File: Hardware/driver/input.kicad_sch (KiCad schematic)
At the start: 55 parts, among them J301 1017526, Q301 IXTH80N075L2, Q302 IXTH80N075L2, U301 MCP3421A2T-ECH, U302 MCP3421A1T-ECH, U303 DAC60501Z, U304 DAC60501Z, U305 DS18B20, U306 DS18B20, U307 MCP3421A3T-ECH, U308 OPA2388, U309 OPA2388

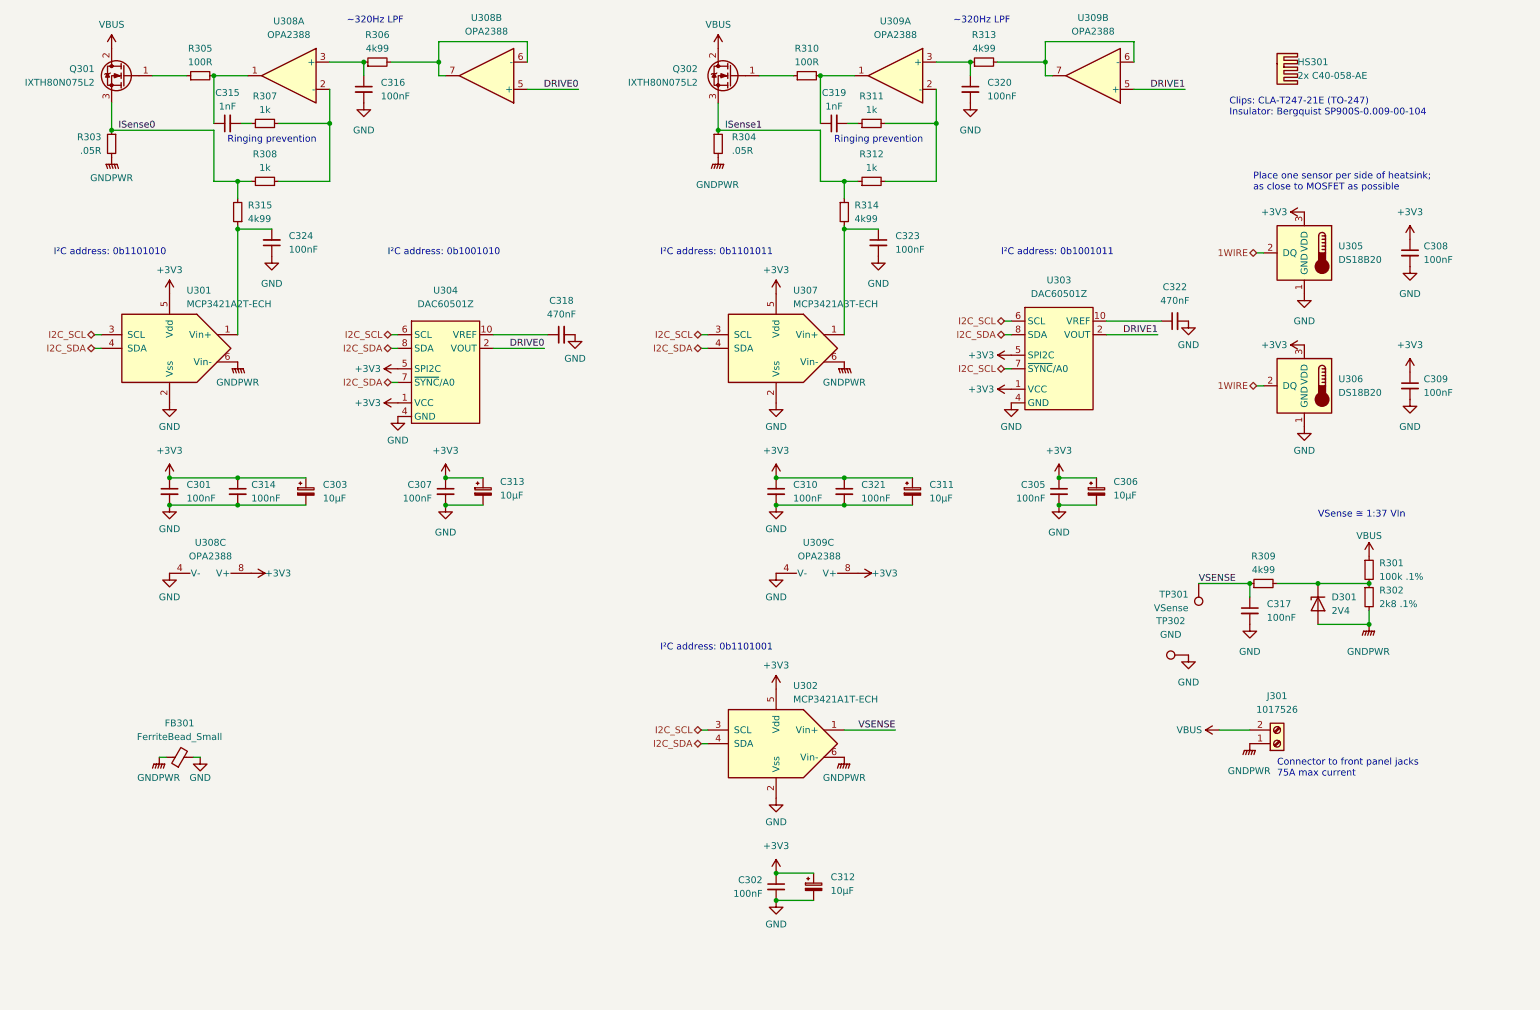
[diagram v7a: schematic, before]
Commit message: Driver current zero adjustment
- Added facility on the driver board to adjust the zero offset for the
  current drive op amps, to allow them to actually reach zero when a
  zero DAC code is input to them.

  This is done by means of a -5V supply (generated with switched
  capacitor regulator) and each output amplifier having a -2.5V
  reference, and an associated multi-turn trim pot to actually trim
  that; these are hooked up to 3V3 digital on the other end (this should
  probably be the DAC reference but we don't have ez access to that)
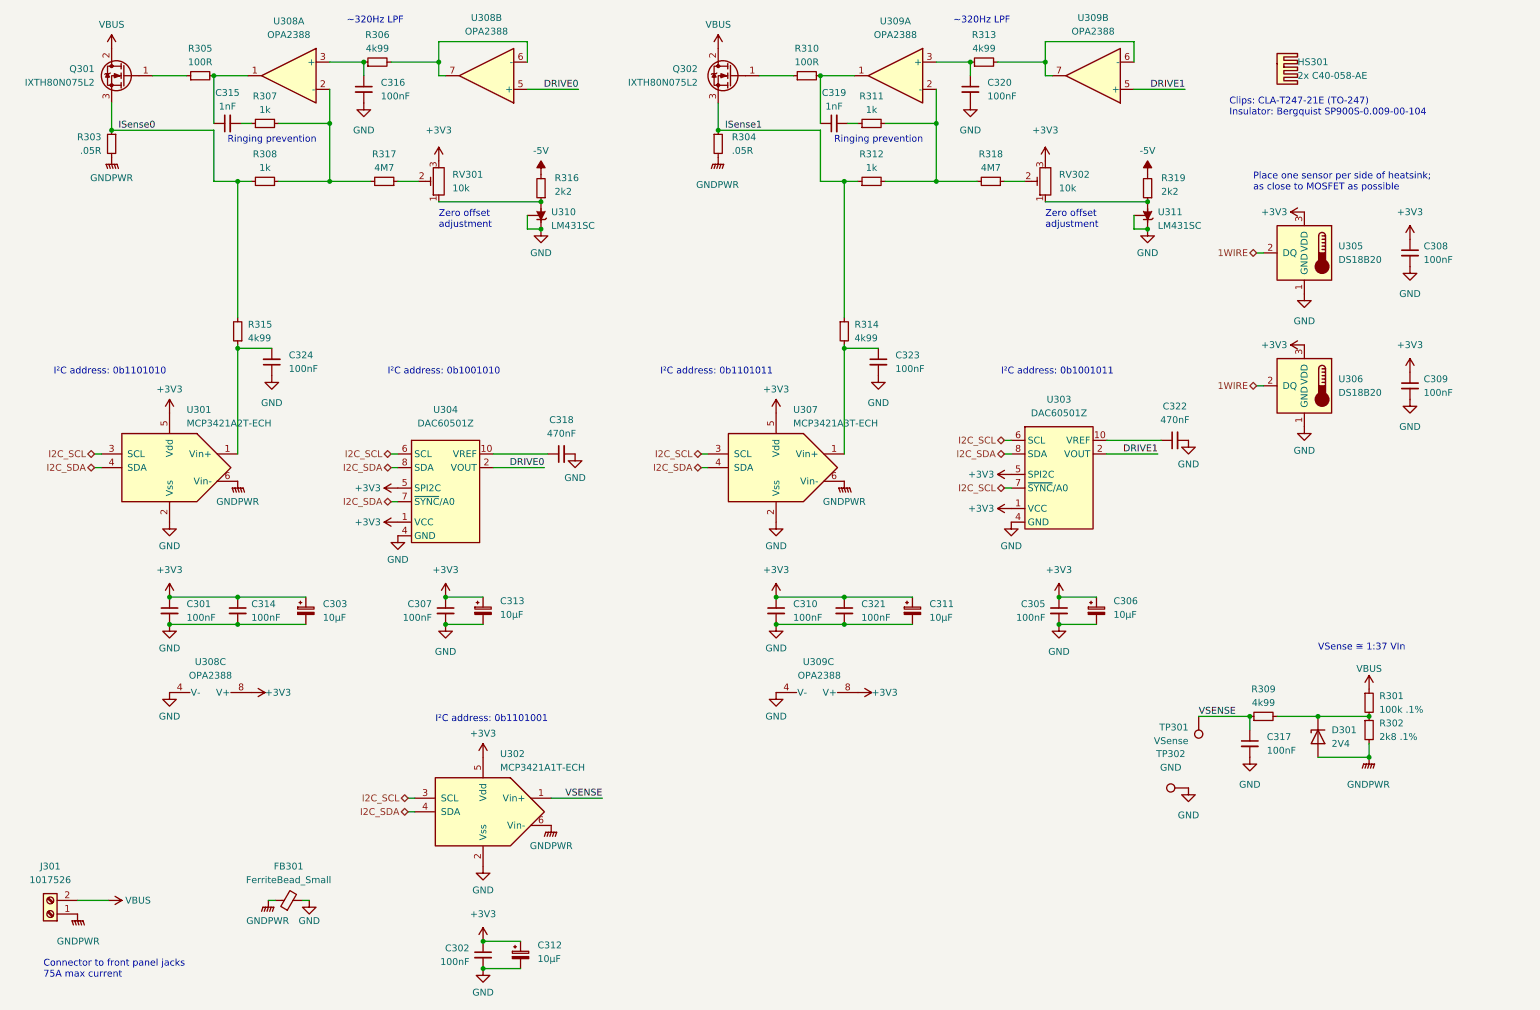
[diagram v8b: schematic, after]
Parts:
- added R316, R319: 2k2, Resistor_SMD:R_0805_2012Metric_Pad1.20x1.40mm_HandSolder, symbol Device:R_Small
- added R317, R318: 4M7, Resistor_SMD:R_0805_2012Metric_Pad1.20x1.40mm_HandSolder, symbol Device:R_Small
- added RV301, RV302: 10k, programmable-load:Potentiometer_Nidec_Copal_CT94EY, symbol Device:R_Potentiometer_Trim
- added U310, U311: LM431SC, Package_TO_SOT_SMD:SOT-23, symbol Reference_Voltage:TL431DBZ
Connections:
- net +3V3: now also RV301.3, RV302.3
- net GND: now also U310.1 (K), U310.2 (REF), U311.1 (K), U311.2 (REF)
- net at R307.2, R308.1, U308.2 (-): now also R317.2
- net at R311.2, R312.2, U309.2 (-): now also R318.2
- new net: R316.1, RV301.1, U310.3 (A)
- new net: R319.1, RV302.1, U311.3 (A)
- new net: R317.1, RV301.2
- new net: R318.1, RV302.2
- new net -5V: R316.2, R319.2
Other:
- note added: "Zero offset adjustment"
- title: (none) -> Dual Programmable Load Driver
- moved on the sheet: C301, C302, C303, C305, C306, C307, C310, C311, C312, C313, C314, C317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
